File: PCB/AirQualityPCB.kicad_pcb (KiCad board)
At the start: 2 copper layers, 100 x 75 mm, 57 parts, among them J1 USB_C_Receptacle_USB2.0_16P, J10 SMA-J-P-H-ST-EM1, J2 TestPoint 5V, J3 TestPoint GND, J4 TestPoint 3.3V, U1 Regulator, U10 INIR2-ME5, U11 110-507, U12 110-303, U13 ESP32-C3-WROOM-02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

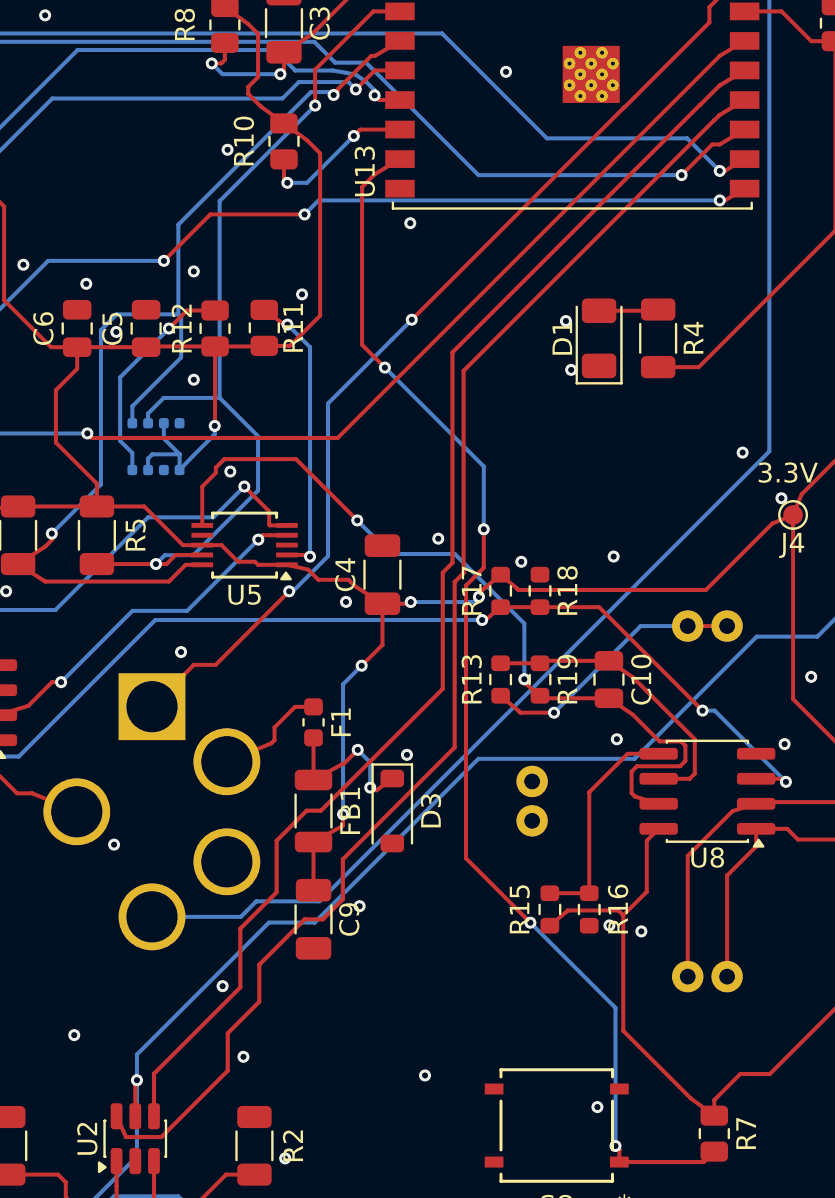
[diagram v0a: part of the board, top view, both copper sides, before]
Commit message: Updated fuse and started work on talking with CH4 sensor
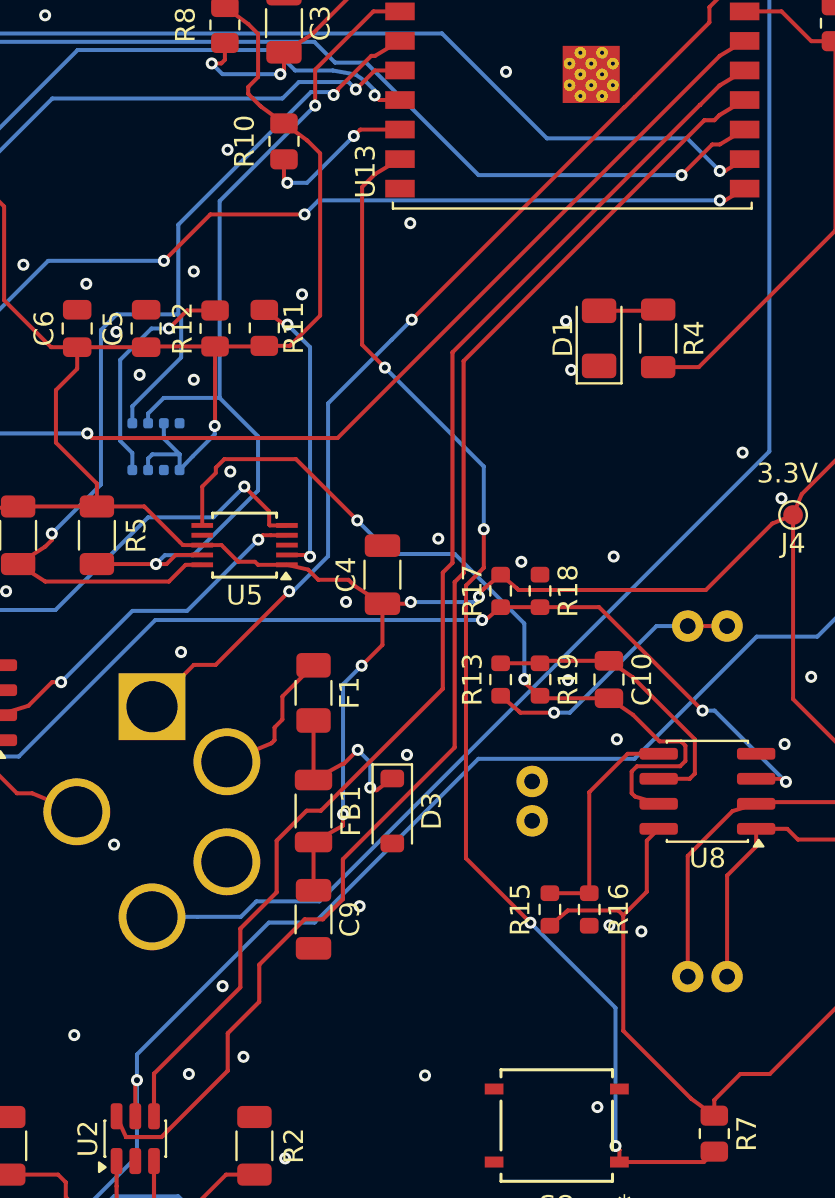
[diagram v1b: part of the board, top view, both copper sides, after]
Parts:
- F1: footprint Fuse:Fuse_0603_1608Metric -> Fuse:Fuse_1206_3216Metric
- moved F1 1.50 mm to (142.1, 89.4)
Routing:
- net Net-(U10-VIN): track 5.73 -> 7.29 mm
- net Net-(D3-K): track 8.44 -> 9.32 mm
- net Net-(U6-SDO): track 11.2 -> 11.7 mm
- net GND: vias 90 -> 93
